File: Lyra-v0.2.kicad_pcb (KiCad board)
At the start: 4 copper layers, 34.9 x 33.3 mm, 56 parts, among them CN1 QWIIC, SW1 Button, SW2 Button, U1 RP2354A, U2 ABM8-272-T3, U3 TPS2121RUXR, U4 TPS62152RGTR, U5 ICM-40609-D, U6 BMP388, U7 SMA-KHD9

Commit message: fix PCB
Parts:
- moved C23 3.19 mm to (141.2, 90.7), turned to 45 degrees
- moved C22 2.89 mm to (141.1, 93.1), turned to -45 degrees
- moved R12 2.19 mm to (143.5, 90.7), turned to -45 degrees
- moved R11 1.61 mm to (143.5, 93.1), turned to -135 degrees
- moved U6 0.91 mm to (142.4, 91.9), turned to -135 degrees
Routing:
- net +3V3: track 105.7 -> 110.4 mm
- net /RP2354A/GPIO6: track 18.4 -> 22.9 mm
- net /RP2354A/GPIO7: track 19.0 -> 22.4 mm
- net +1V1: track 17.6 -> 18.1 mm
- net GND: vias 83 -> 89
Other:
- outline, holes or cut-outs redrawn

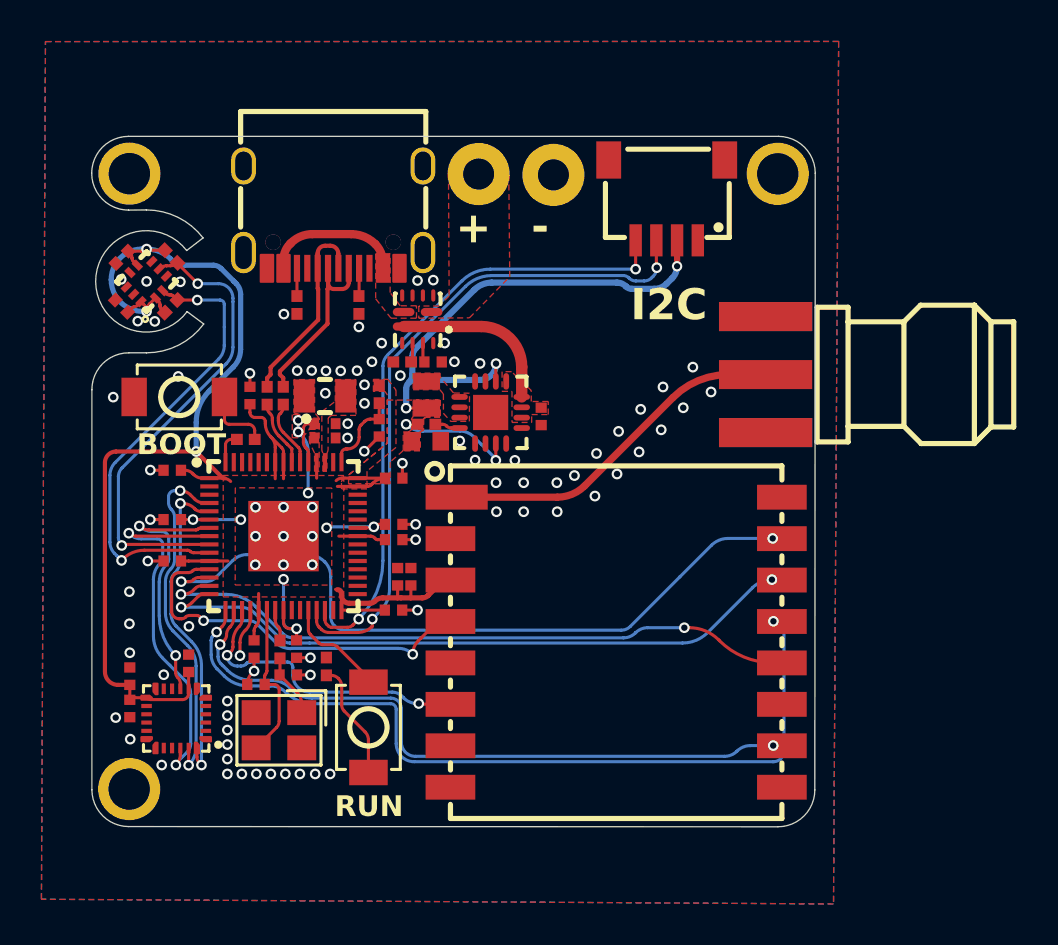
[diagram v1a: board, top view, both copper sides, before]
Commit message: switched to RP2350A and added flash chip due to parts shortage
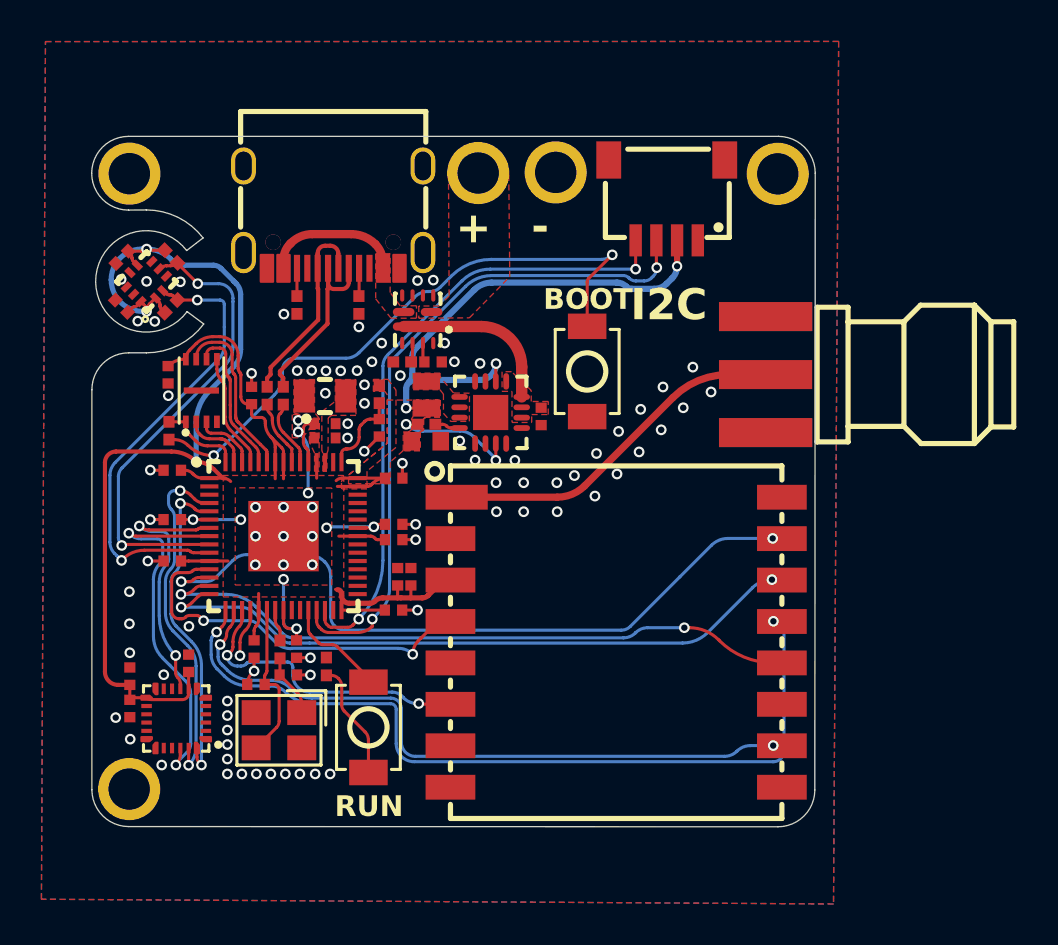
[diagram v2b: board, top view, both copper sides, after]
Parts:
- removed ?: , 
- removed REF**: M2_Hole, Other:M2_Hole
- added C26: 1uF, Capacitors:C0402, F.Cu at (143.4, 96.4)
- added M4: ~, Other:M2_Hole, F.Cu at (158.4, 86.6)
- added M5: ~, Other:M2_Hole, F.Cu at (162.1, 86.5)
- added U8: W25Q16JVUXIQ, Other:USON-8_L3.0-W2.0-P0.50-BL-EP, F.Cu at (145.0, 97.1)
- U1: value RP2354A -> RP2350A
- moved SW1 19.7 mm to (163.6, 96.2), turned to 90 degrees
- moved R6 3.73 mm to (143.4, 99.1), turned to 90 degrees
- moved C4 0.08 mm to (147.4, 97.4)
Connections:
- net Net-(U1-QSPI_SS) renamed /RP2354A/QSPI_SS
- U1 pad 55: unconnected-(U1-QSPI_SD3-Pad55) -> /RP2354A/QSPI_SD3
- U1 pad 56: unconnected-(U1-QSPI_SCLK-Pad56) -> /RP2354A/QSPI_SCLK
- U1 pad 57: unconnected-(U1-QSPI_SD0-Pad57) -> /RP2354A/QSPI_SD0
- U1 pad 58: unconnected-(U1-QSPI_SD2-Pad58) -> /RP2354A/QSPI_SD2
- U1 pad 59: unconnected-(U1-QSPI_SD1-Pad59) -> /RP2354A/QSPI_SD1
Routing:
- net Net-(R6-Pad1): track 3.26 -> 29.7 mm, vias 0 -> 2
- net /RP2354A/QSPI_SD3: track 0.00 -> 8.36 mm
- net +3V3: track 110.4 -> 118.0 mm
- net /RP2354A/QSPI_SCLK: track 0.00 -> 7.29 mm
- net /RP2354A/QSPI_SD0: track 0.00 -> 5.52 mm
- net /RP2354A/QSPI_SD1: track 0.00 -> 3.18 mm
- net /RP2354A/QSPI_SD2: track 0.00 -> 3.07 mm
- net /RP2354A/QSPI_SS: track 1.52 -> 4.06 mm
- net GND: vias 89 -> 88

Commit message: Final manufactured version
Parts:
- removed C26: 1uF, Capacitors:C0402
- removed M4, M5: ~, Other:M2_Hole
- removed U8: W25Q16JVUXIQ, Other:USON-8_L3.0-W2.0-P0.50-BL-EP
- added ?: , , F.Cu at (162.0, 86.7)
- added REF**: M2_Hole, Other:M2_Hole, F.Cu at (158.5, 86.7)
- U1: value RP2350A -> RP2354A
- moved SW1 19.7 mm to (143.9, 97.5), turned to 0 degrees
- moved R6 3.73 mm to (147.2, 99.5), turned to 180 degrees
- moved C4 0.08 mm to (147.3, 97.4)
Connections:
- net /RP2354A/QSPI_SS renamed Net-(U1-QSPI_SS)
- U1 pad 55: /RP2354A/QSPI_SD3 -> unconnected-(U1-QSPI_SD3-Pad55)
- U1 pad 56: /RP2354A/QSPI_SCLK -> unconnected-(U1-QSPI_SCLK-Pad56)
- U1 pad 57: /RP2354A/QSPI_SD0 -> unconnected-(U1-QSPI_SD0-Pad57)
- U1 pad 58: /RP2354A/QSPI_SD2 -> unconnected-(U1-QSPI_SD2-Pad58)
- U1 pad 59: /RP2354A/QSPI_SD1 -> unconnected-(U1-QSPI_SD1-Pad59)
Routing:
- net Net-(R6-Pad1): track 29.7 -> 3.26 mm, vias 2 -> 0
- net /RP2354A/QSPI_SD3: track 8.36 -> 0.00 mm
- net /RP2354A/QSPI_SCLK: track 7.29 -> 0.00 mm
- net +3V3: track 118.0 -> 110.8 mm
- net /RP2354A/QSPI_SD0: track 5.52 -> 0.00 mm
- net /RP2354A/QSPI_SD1: track 3.18 -> 0.00 mm
- net /RP2354A/QSPI_SD2: track 3.07 -> 0.00 mm
- net Net-(U1-QSPI_SS): track 4.06 -> 1.52 mm
- net GND: vias 88 -> 89
